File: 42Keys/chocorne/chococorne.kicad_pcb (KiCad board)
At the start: 2 copper layers, 130 x 87.7 mm, 63 parts, among them J1 MJ-4PP-9, J2 OLED, SW1 SW_PUSH, SW10 SW_PUSH, SW11 SW_PUSH, SW12 SW_PUSH, SW13 SW_PUSH, SW14 SW_PUSH, SW15 SW_PUSH, SW16 SW_PUSH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

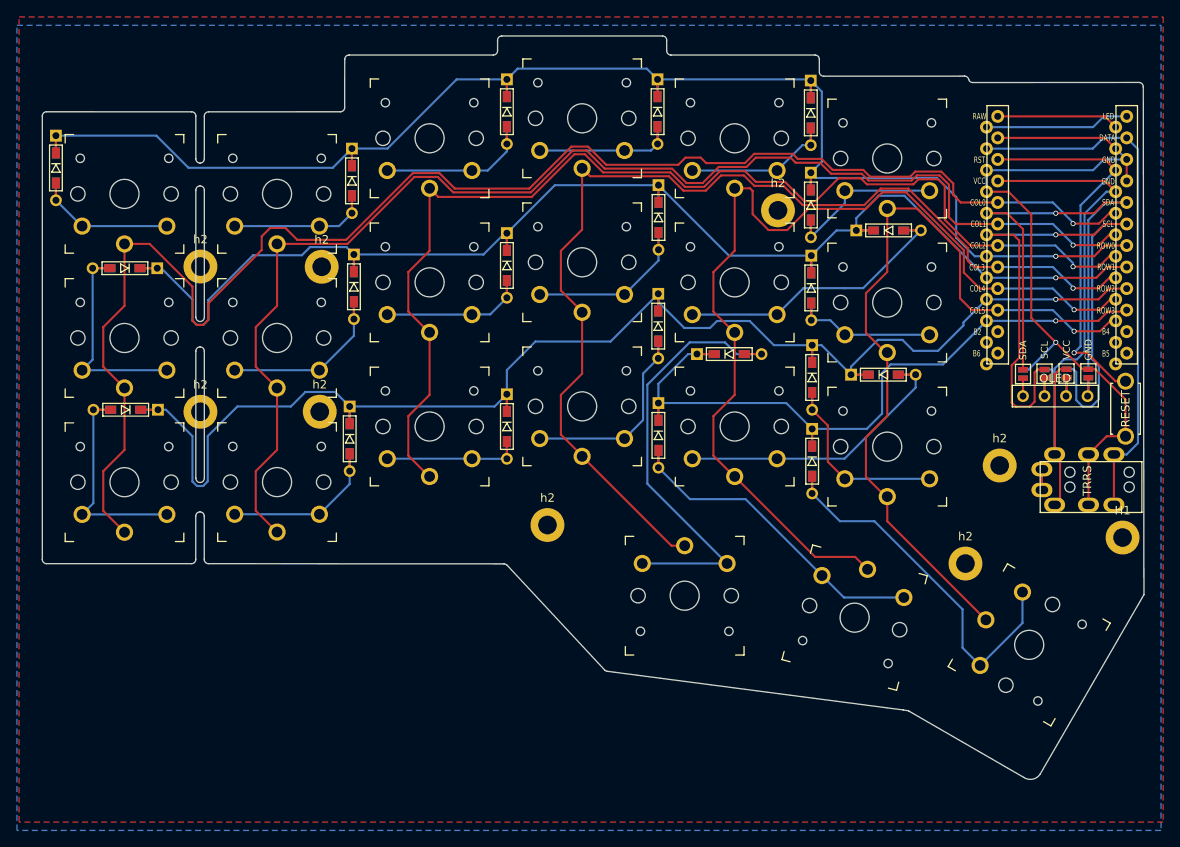
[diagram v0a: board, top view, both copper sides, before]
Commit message: Increse drill hole size for chocorne and reroute
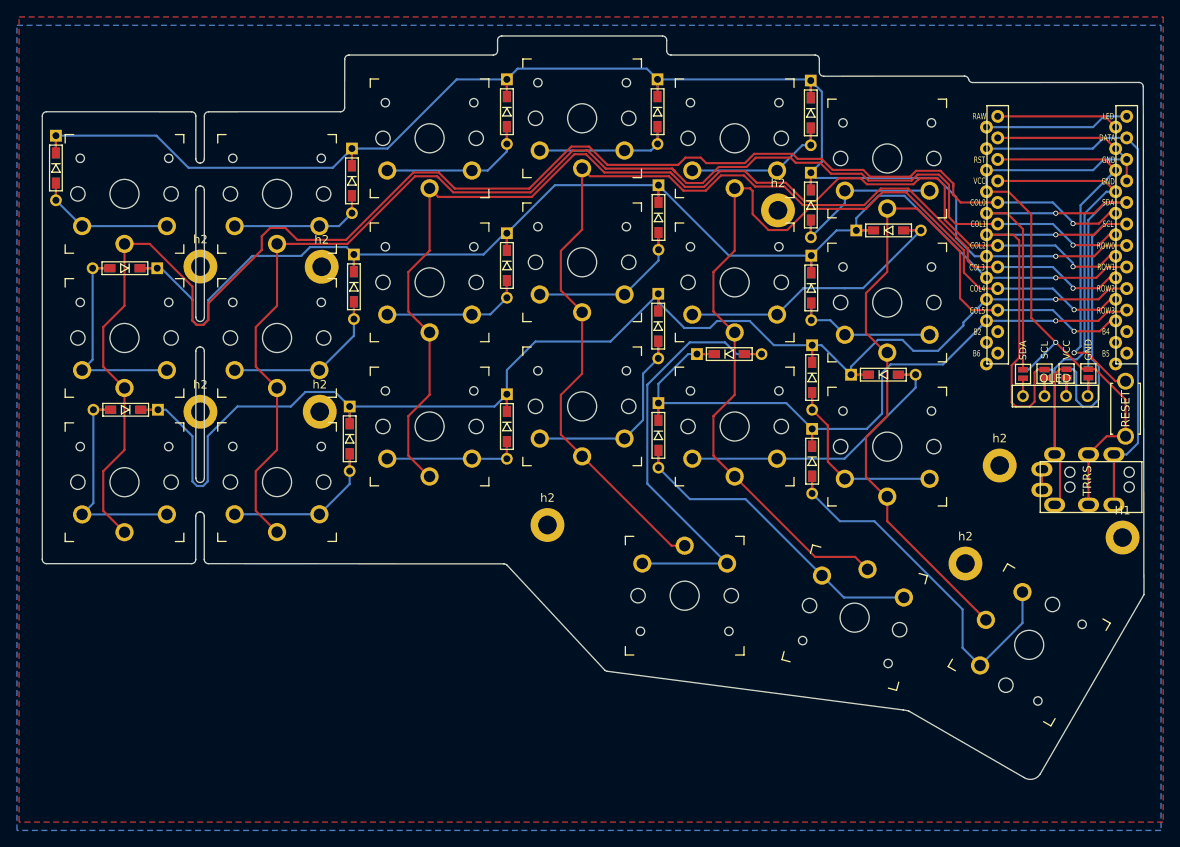
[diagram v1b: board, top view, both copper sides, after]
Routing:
- net col1: track 153.5 -> 154.3 mm
